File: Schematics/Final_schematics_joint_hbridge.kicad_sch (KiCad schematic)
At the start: 42 parts, among them J1 FVOL, J2 RVOL, J3 L-R, J4 ISP_Alike, J5 Conn_01x02_Pin, J6 F-R, J7 Header, Q5 Q_PMOS, Q6 Q_NMOS_GDS, Q7 Q_PMOS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

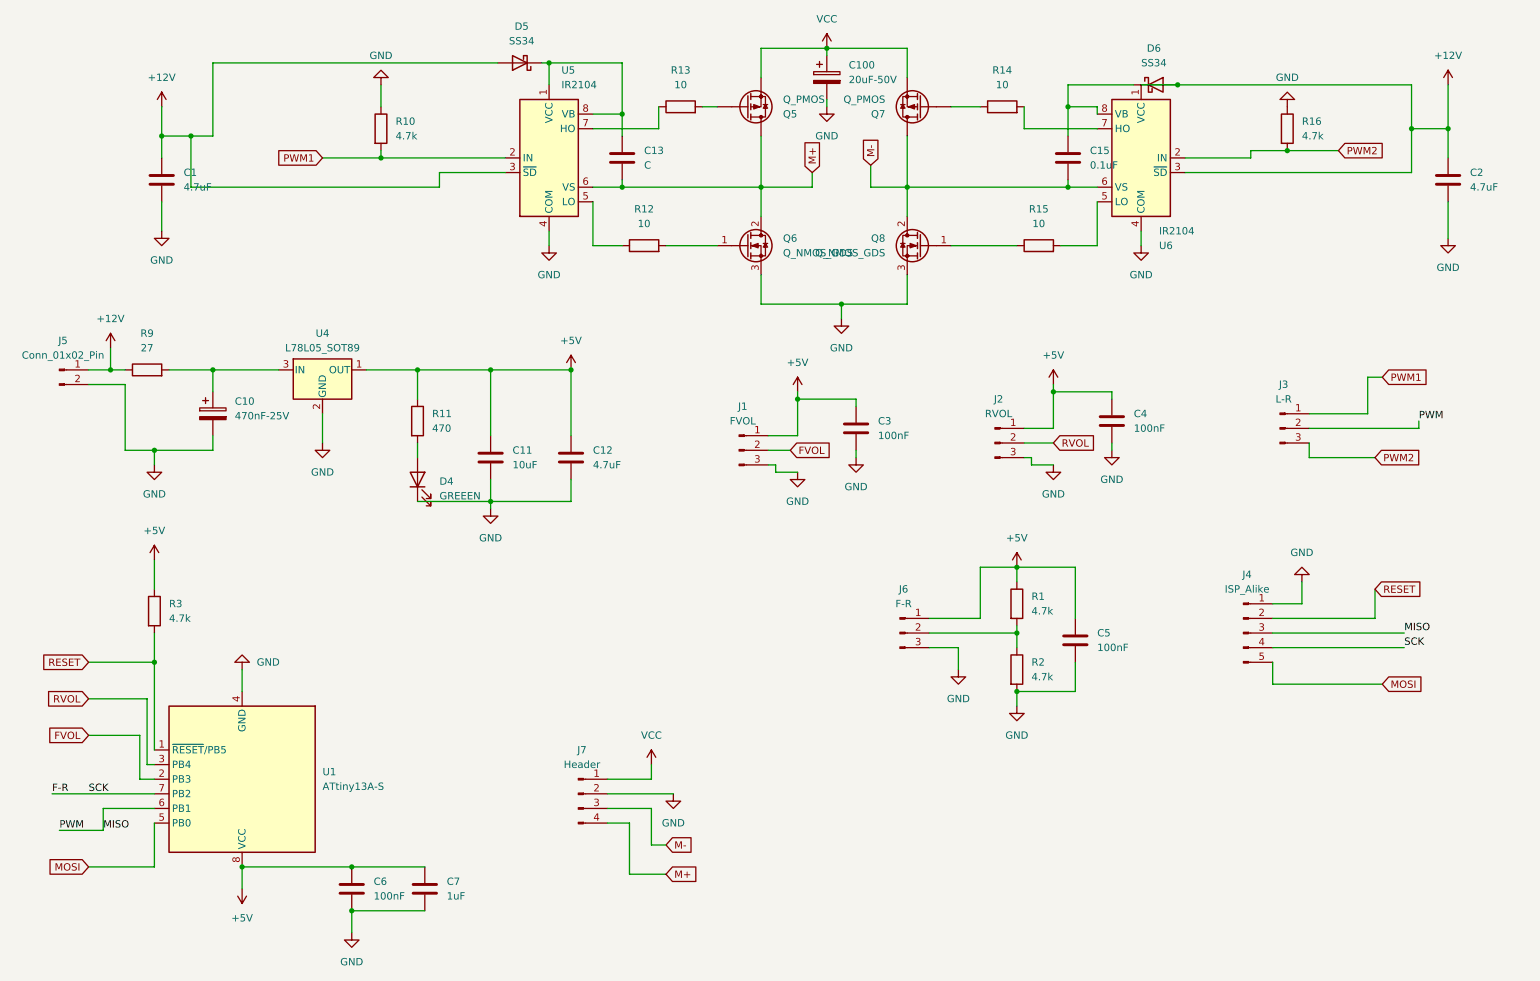
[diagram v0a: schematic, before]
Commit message: Revised schematic with KiCAD
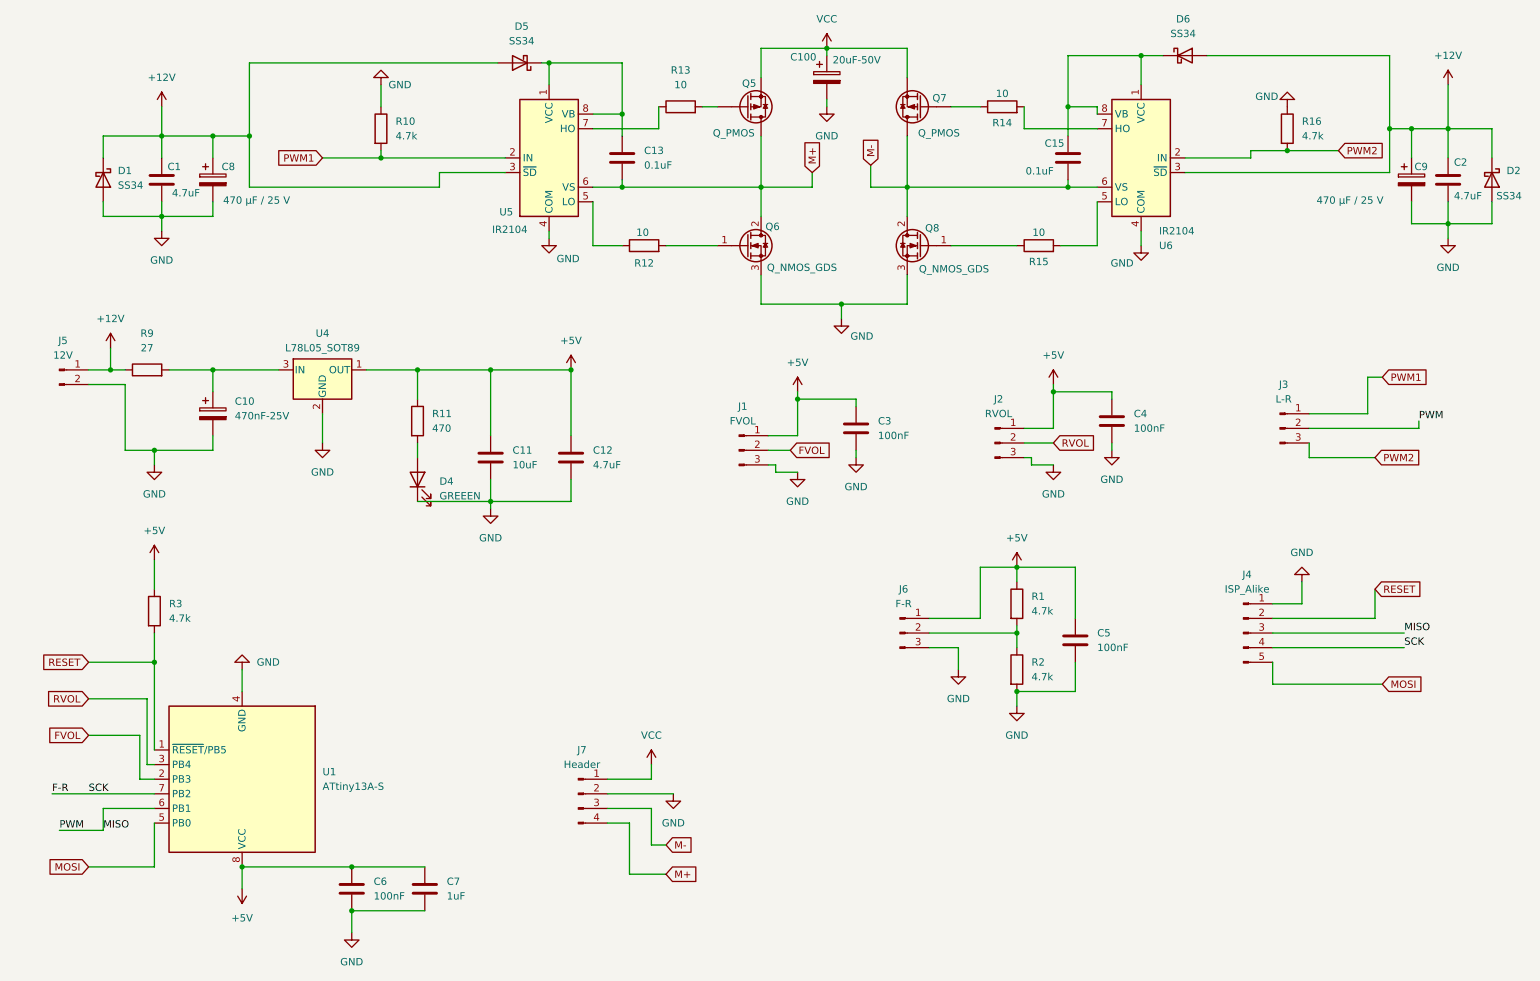
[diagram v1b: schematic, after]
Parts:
- added C8, C9: 470 µF / 25 V, symbol Device:C_Polarized
- added D1, D2: SS34, Diode_SMD:D_SMA, symbol Diode:SS34
- C13: value C -> 0.1uF
- J5: value Conn_01x02_Pin -> 12V
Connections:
- net +12V: now also C8.1, C9.1, D1.1 (K), D2.1 (K); no longer U6.1 (VCC)
- net GND: now also C8.2, C9.2, D1.2 (A), D2.2 (A)
- net at C15.1, D6.1 (K), U6.8 (VB): now also U6.1 (VCC)
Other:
- moved on the sheet: D6

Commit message: Resolve merge conflicts
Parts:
- added J8: Conn_01x01_Pin, symbol Connector:Conn_01x01_Pin
- added R_shunt: 0.05, symbol Device:R
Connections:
- net GND: now also R_shunt.2; no longer Q6.3 (S), Q8.3 (S)
- new net TorqueSensor: J8.1 (Pin_1), Q6.3 (S), Q8.3 (S), R_shunt.1
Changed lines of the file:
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@@
 	)
 	(junction
+		(at 165.1 72.39)
+		(diameter 0)
+		(color 0 0 0 0)
+	)
+	(junction
 		(at 91.44 83.82)
 		(diameter 0)
@@
 	)
 	(junction
-		(at 165.1 72.39)
+		(at 165.1 73.66)
 		(diameter 0)
 		(color 0 0 0 0)
@@
 	(wire
 		(pts
-			(xy 165.1 72.39) (xy 176.53 72.39)
-		)
-		(stroke
-			(width 0)
-			(type default)
-		)
-	)
-	(wire
-		(pts
 			(xy 195.58 118.11) (xy 195.58 120.65)
 		)
@@
 	(wire
 		(pts
+			(xy 250.19 76.2) (xy 257.81 76.2)
+		)
+		(stroke
+			(width 0)
+			(type default)
+		)
+	)
+	(wire
+		(pts
 			(xy 185.42 132.08) (xy 185.42 135.89)
 		)
@@
 	(wire
 		(pts
-			(xy 165.1 72.39) (xy 165.1 74.93)
-		)
-		(stroke
-			(width 0)
-			(type default)
-		)
-	)
-	(wire
-		(pts
 			(xy 278.13 46.99) (xy 278.13 41.91)
 		)
@@
 	(wire
 		(pts
+			(xy 165.1 73.66) (xy 182.88 73.66)
+		)
+		(stroke
+			(width 0)
+			(type default)
+		)
+	)
+	(wire
+		(pts
+			(xy 165.1 72.39) (xy 165.1 73.66)
+		)
+		(stroke
+			(width 0)
+			(type default)
+		)
+	)
+	(wire
+		(pts
 			(xy 132.08 166.37) (xy 134.62 166.37)
 		)
@@
 	(wire
 		(pts
+			(xy 165.1 81.28) (xy 165.1 83.82)
+		)
+		(stroke
+			(width 0)
+			(type default)
+		)
+	)
+	(wire
+		(pts
 			(xy 265.43 92.71) (xy 265.43 93.98)
 		)
@@
 	(wire
 		(pts
+			(xy 165.1 72.39) (xy 176.53 72.39)
+		)
+		(stroke
+			(width 0)
+			(type default)
+		)
+	)
+	(wire
+		(pts
 			(xy 240.03 138.43) (xy 259.08 138.43)
 		)
@@
 		)
 	)
+	(global_label "TorqueSensor"
+		(shape input)
+		(at 182.88 73.66 0)
+		(fields_autoplaced yes)
+		(effects
+			(font
+				(size 1.27 1.27)
+			)
+			(justify left)
+		)
+		(property "Intersheetrefs" "${INTERSHEET_REFS}"
+			(at 198.565 73.66 0)
+			(effects
+				(font
+					(size 1.27 1.27)
+				)
+				(justify left)
+				(hide yes)
+			)
+		)
+	)
 	(global_label "M-"
 		(shape input)
@@
 		)
 	)
+	(global_label "TorqueSensor"
+		(shape input)
+		(at 257.81 76.2 0)
+		(fields_autoplaced yes)
+		(effects
+			(font
+				(size 1.27 1.27)
+			)
+			(justify left)
+		)
+		(property "Intersheetrefs" "${INTERSHEET_REFS}"
+			(at 273.495 76.2 0)
+			(effects
+				(font
+					(size 1.27 1.27)
+				)
+				(justify left)
+				(hide yes)
+			)
+		)
+	)
 	(global_label "RVOL"
 		(shape input)
@@
 	(symbol
 		(lib_id "power:GND")
-		(at 165.1 74.93 0)
+		(at 165.1 83.82 0)
 		(unit 1)
 		(exclude_from_sim no)
@@
 		(dnp no)
 		(property "Reference" "#PWR028"
-			(at 165.1 81.28 0)
+			(at 165.1 90.17 0)
 			(effects
 				(font
@@
 		)
 		(property "Value" "GND"
-			(at 168.656 77.978 0)
+			(at 168.656 86.868 0)
 			(effects
 				(font
@@
 		)
 		(property "Footprint" ""
-			(at 165.1 74.93 0)
+			(at 165.1 83.82 0)
 			(effects
 				(font
@@
 		)
 		(property "Datasheet" ""
-			(at 165.1 74.93 0)
+			(at 165.1 83.82 0)
 			(effects
 				(font
@@
 		)
 		(property "Description" "Power symbol creates a global label with name \"GND\" , ground"
-			(at 165.1 74.93 0)
+			(at 165.1 83.82 0)
 			(effects
 				(font
@@
 	)
 	(symbol
+		(lib_id "Device:R")
+		(at 165.1 77.47 0)
+		(unit 1)
+		(exclude_from_sim no)
+		(in_bom yes)
+		(on_board yes)
+		(dnp no)
+		(fields_autoplaced yes)
+		(property "Reference" "R_shunt"
+			(at 167.64 76.1999 0)
+			(effects
+				(font
+					(size 1.27 1.27)
+				)
+				(justify left)
+			)
+		)
+		(property "Value" "0.05"
+			(at 167.64 78.7399 0)
+			(effects
+				(font
+					(size 1.27 1.27)
+				)
+				(justify left)
+			)
+		)
+		(property "Footprint" ""
+			(at 163.322 77.47 90)
+			(effects
+				(font
+					(size 1.27 1.27)
+				)
+				(hide yes)
+			)
+		)
+		(property "Datasheet" "~"
+			(at 165.1 77.47 0)
+			(effects
+				(font
+					(size 1.27 1.27)
+				)
+				(hide yes)
+			)
+		)
+		(property "Description" "Resistor"
+			(at 165.1 77.47 0)
+			(effects
+				(font
+					(size 1.27 1.27)
+				)
+				(hide yes)
+			)
+		)
+		(pin "2"
+		)
+		(pin "1"
+		)
+		(instances
+			(project ""
+				(path "/6b1e787a-9a3a-4b4c-81e6-12224e330815"
+					(reference "R_shunt")
+					(unit 1)
+				)
+			)
+		)
+	)
+	(symbol
 		(lib_id "power:GND")
 		(at 135.89 157.48 0)
@@
 					(unit 1)
 				)
+			)
+		)
+	)
+	(symbol
+		(lib_id "Connector:Conn_01x01_Pin")
+		(at 245.11 76.2 0)
+		(unit 1)
+		(exclude_from_sim no)
+		(in_bom yes)
+		(on_board yes)
+		(dnp no)
+		(fields_autoplaced yes)
+		(property "Reference" "J8"
+			(at 245.745 71.12 0)
+			(effects
+				(font
+					(size 1.27 1.27)
+				)
+			)
+		)
+		(property "Value" "Conn_01x01_Pin"
+			(at 245.745 73.66 0)
+			(effects
+				(font
+					(size 1.27 1.27)
+				)
+			)
+		)
+		(property "Footprint" ""
+			(at 245.11 76.2 0)
+			(effects
+				(font
+					(size 1.27 1.27)
+				)
+				(hide yes)
+			)
+		)
+		(property "Datasheet" "~"
+			(at 245.11 76.2 0)
+			(effects
+				(font
+					(size 1.27 1.27)
+				)
+				(hide yes)
+			)
+		)
+		(property "Description" "Generic connector, single row, 01x01, script generated"
+			(at 245.11 76.2 0)
+			(effects
+				(font
+					(size 1.27 1.27)
+				)
+				(hide yes)
+			)
+		)
+		(pin "1"
+		)
+		(instances
+			(project ""
+				(path "/6b1e787a-9a3a-4b4c-81e6-12224e330815"
+					(reference "J8")
+					(unit 1)
+				)

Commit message: Resolve merge conflicts
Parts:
- removed J8: Conn_01x01_Pin, symbol Connector:Conn_01x01_Pin
- added TorqueSensor: V_shunt, symbol Connector:Conn_01x02_Pin
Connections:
- net GND: now also TorqueSensor.2 (Pin_2)
- net TorqueSensor: now also TorqueSensor.1 (Pin_1)
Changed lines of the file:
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@@
 	(wire
 		(pts
-			(xy 250.19 76.2) (xy 257.81 76.2)
+			(xy 185.42 132.08) (xy 185.42 135.89)
 		)
 		(stroke
@@
 	(wire
 		(pts
-			(xy 185.42 132.08) (xy 185.42 135.89)
+			(xy 45.72 154.94) (xy 43.18 154.94)
 		)
 		(stroke
@@
 	(wire
 		(pts
-			(xy 45.72 154.94) (xy 43.18 154.94)
+			(xy 134.62 62.23) (xy 143.51 62.23)
 		)
 		(stroke
@@
 	(wire
 		(pts
-			(xy 134.62 62.23) (xy 143.51 62.23)
+			(xy 204.47 52.07) (xy 209.55 52.07)
 		)
 		(stroke
@@
 	(wire
 		(pts
-			(xy 204.47 52.07) (xy 209.55 52.07)
+			(xy 246.38 72.39) (xy 250.19 72.39)
 		)
 		(stroke
@@
 	(wire
 		(pts
+			(xy 246.38 74.93) (xy 250.19 74.93)
+		)
+		(stroke
+			(width 0)
+			(type default)
+		)
+	)
+	(wire
+		(pts
 			(xy 198.12 100.33) (xy 201.93 100.33)
 		)
@@
 	(wire
 		(pts
+			(xy 250.19 74.93) (xy 250.19 76.2)
+		)
+		(stroke
+			(width 0)
+			(type default)
+		)
+	)
+	(wire
+		(pts
 			(xy 184.15 38.1) (xy 189.23 38.1)
 		)
@@
 	(global_label "TorqueSensor"
 		(shape input)
-		(at 257.81 76.2 0)
+		(at 250.19 72.39 0)
 		(fields_autoplaced yes)
 		(effects
@@
 		)
 		(property "Intersheetrefs" "${INTERSHEET_REFS}"
-			(at 273.495 76.2 0)
+			(at 265.875 72.39 0)
 			(effects
 				(font
@@
 	)
 	(symbol
+		(lib_id "Connector:Conn_01x02_Pin")
+		(at 241.3 72.39 0)
+		(unit 1)
+		(exclude_from_sim no)
+		(in_bom yes)
+		(on_board yes)
+		(dnp no)
+		(fields_autoplaced yes)
+		(property "Reference" "TorqueSensor"
+			(at 241.935 67.31 0)
+			(effects
+				(font
+					(size 1.27 1.27)
+				)
+			)
+		)
+		(property "Value" "V_shunt"
+			(at 241.935 69.85 0)
+			(effects
+				(font
+					(size 1.27 1.27)
+				)
+			)
+		)
+		(property "Footprint" ""
+			(at 241.3 72.39 0)
+			(effects
+				(font
+					(size 1.27 1.27)
+				)
+				(hide yes)
+			)
+		)
+		(property "Datasheet" "~"
+			(at 241.3 72.39 0)
+			(effects
+				(font
+					(size 1.27 1.27)
+				)
+				(hide yes)
+			)
+		)
+		(property "Description" "Generic connector, single row, 01x02, script generated"
+			(at 241.3 72.39 0)
+			(effects
+				(font
+					(size 1.27 1.27)
+				)
+				(hide yes)
+			)
+		)
+		(pin "1"
+		)
+		(pin "2"
+		)
+		(instances
+			(project "joint_hbridge"
+				(path "/6b1e787a-9a3a-4b4c-81e6-12224e330815"
+					(reference "TorqueSensor")
+					(unit 1)
+				)
+			)
+		)
+	)
+	(symbol
 		(lib_id "Device:R")
 		(at 165.1 77.47 0)
@@
 	)
 	(symbol
-		(lib_id "Connector:Conn_01x01_Pin")
-		(at 245.11 76.2 0)
+		(lib_id "Device:C")
+		(at 205.74 130.81 0)
 		(unit 1)
 		(exclude_from_sim no)
@@
 		(dnp no)
 		(fields_autoplaced yes)
-		(property "Reference" "J8"
-			(at 245.745 71.12 0)
+		(property "Reference" "C5"
+			(at 209.55 129.5399 0)
 			(effects
 				(font
 					(size 1.27 1.27)
 				)
+				(justify left)
 			)
 		)
-		(property "Value" "Conn_01x01_Pin"
-			(at 245.745 73.66 0)
+		(property "Value" "100nF"
+			(at 209.55 132.0799 0)
 			(effects
 				(font
 					(size 1.27 1.27)
 				)
+				(justify left)
 			)
 		)
 		(property "Footprint" ""
-			(at 245.11 76.2 0)
+			(at 206.7052 134.62 0)
 			(effects
 				(font
@@
 		)
 		(property "Datasheet" "~"
-			(at 245.11 76.2 0)
+			(at 205.74 130.81 0)
 			(effects
 				(font
@@
 			)
 		)
-		(property "Description" "Generic connector, single row, 01x01, script generated"
-			(at 245.11 76.2 0)
+		(property "Description" "Unpolarized capacitor"
+			(at 205.74 130.81 0)
 			(effects
 				(font
@@
 		(pin "1"
 		)
+		(pin "2"
+		)
 		(instances
-			(project ""
+			(project "joint_hbridge"
 				(path "/6b1e787a-9a3a-4b4c-81e6-12224e330815"
-					(reference "J8")
+					(reference "C5")
 					(unit 1)
 				)
@@
 	)
 	(symbol
-		(lib_id "Device:C")
-		(at 205.74 130.81 0)
+		(lib_id "Connector:Conn_01x03_Pin")
+		(at 147.32 97.79 0)
 		(unit 1)
 		(exclude_from_sim no)
@@
 		(dnp no)
 		(fields_autoplaced yes)
-		(property "Reference" "C5"
-			(at 209.55 129.5399 0)
+		(property "Reference" "J1"
+			(at 147.955 90.17 0)
 			(effects
 				(font
 					(size 1.27 1.27)
 				)
-				(justify left)
 			)
 		)
-		(property "Value" "100nF"
-			(at 209.55 132.0799 0)
+		(property "Value" "FVOL"
+			(at 147.955 92.71 0)
 			(effects
 				(font
 					(size 1.27 1.27)
 				)
-				(justify left)
 			)
 		)
 		(property "Footprint" ""
-			(at 206.7052 134.62 0)
+			(at 147.32 97.79 0)
 			(effects
 				(font
@@
 		)
 		(property "Datasheet" "~"
-			(at 205.74 130.81 0)
+			(at 147.32 97.79 0)
 			(effects
 				(font
@@
 			)
 		)
-		(property "Description" "Unpolarized capacitor"
-			(at 205.74 130.81 0)
+		(property "Description" "Generic connector, single row, 01x03, script generated"
+			(at 147.32 97.79 0)
 			(effects
 				(font
@@
 		(pin "1"
 		)
+		(pin "3"
+		)
 		(pin "2"
 		)
 		(instances
-			(project "joint_hbridge"
+			(project ""
 				(path "/6b1e787a-9a3a-4b4c-81e6-12224e330815"
-					(reference "C5")
+					(reference "J1")
 					(unit 1)
 				)
@@
 	)
 	(symbol
-		(lib_id "Connector:Conn_01x03_Pin")
-		(at 147.32 97.79 0)
+		(lib_id "power:GND")
+		(at 250.19 76.2 0)
 		(unit 1)
 		(exclude_from_sim no)
@@
 		(on_board yes)
 		(dnp no)
-		(fields_autoplaced yes)
-		(property "Reference" "J1"
-			(at 147.955 90.17 0)
+		(property "Reference" "#PWR033"
+			(at 250.19 82.55 0)
 			(effects
 				(font
 					(size 1.27 1.27)
 				)
+				(hide yes)
 			)
 		)
-		(property "Value" "FVOL"
-			(at 147.955 92.71 0)
+		(property "Value" "GND"
+			(at 253.746 79.248 0)
 			(effects
 				(font
@@
 		)
 		(property "Footprint" ""
-			(at 147.32 97.79 0)
+			(at 250.19 76.2 0)
 			(effects
 				(font
@@
 			)
 		)
-		(property "Datasheet" "~"
-			(at 147.32 97.79 0)
+		(property "Datasheet" ""
+			(at 250.19 76.2 0)
 			(effects
 				(font
@@
 			)
 		)
-		(property "Description" "Generic connector, single row, 01x03, script generated"
-			(at 147.32 97.79 0)
+		(property "Description" "Power symbol creates a global label with name \"GND\" , ground"
+			(at 250.19 76.2 0)
 			(effects
 				(font
@@
 		(pin "1"
 		)
-		(pin "3"
-		)
-		(pin "2"
-		)
 		(instances
-			(project ""
+			(project "joint_hbridge"
 				(path "/6b1e787a-9a3a-4b4c-81e6-12224e330815"
-					(reference "J1")
+					(reference "#PWR033")
 					(unit 1)
 				)

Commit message: Resolve merge conflicts
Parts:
- removed Q5, Q7: Q_PMOS, symbol Device:Q_PMOS
- added D3, D7, D8, D9: SS36, Diode_SMD:D_SMA, symbol Diode:SS36
- added Q1, Q2: Q_NMOS_GDS, symbol Transistor_FET:Q_NMOS_GDS
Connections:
- net M+: now also D3.2 (A), D9.1 (K), Q1.2 (D)
- net M-: now also D7.2 (A), D8.1 (K), Q2.2 (D)
- net TorqueSensor: now also D8.2 (A), D9.2 (A)
- net VCC: now also D3.1 (K), D7.1 (K), Q1.3 (S), Q2.3 (S)
- net at R13.2: now also Q1.1 (G)
- net at R14.1: now also Q2.1 (G)

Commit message: Resolve merge conflicts
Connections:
- net M+: now also Q1.3 (S); no longer Q1.2 (D)
- net M-: now also Q2.3 (S); no longer Q2.2 (D)
- net VCC: now also Q1.2 (D), Q2.2 (D); no longer Q1.3 (S), Q2.3 (S)
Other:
- moved on the sheet: Q2
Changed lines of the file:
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@@
 		(lib_id "Transistor_FET:Q_NMOS_GDS")
 		(at 148.59 38.1 0)
-		(mirror x)
 		(unit 1)
 		(exclude_from_sim no)
@@
 		(dnp no)
 		(property "Reference" "Q1"
-			(at 151.892 41.402 0)
+			(at 151.892 34.798 0)
 			(effects
 				(font
@@
 		)
 		(property "Value" "Q_NMOS_GDS"
-			(at 152.146 34.29 0)
-			(effects
-				(font
-					(size 1.27 1.27)
-				)
-				(justify left)
-			)
-		)
-		(property "Footprint" ""
-			(at 153.67 40.64 0)
+			(at 152.146 41.91 0)
+			(effects
+				(font
+					(size 1.27 1.27)
+				)
+				(justify left)
+			)
+		)
+		(property "Footprint" ""
+			(at 153.67 35.56 0)
 			(effects
 				(font
@@
 	(symbol
 		(lib_id "Transistor_FET:Q_NMOS_GDS")
-		(at 179.07 38.1 180)
+		(at 179.07 38.1 0)
+		(mirror y)
 		(unit 1)
 		(exclude_from_sim no)
@@
 		(dnp no)
 		(property "Reference" "Q2"
-			(at 182.118 41.148 0)
+			(at 182.118 35.052 0)
 			(effects
 				(font
@@
 		)
 		(property "Value" "Q_NMOS_GDS"
-			(at 190.754 34.036 0)
-			(effects
-				(font
-					(size 1.27 1.27)
-				)
-				(justify left)
-			)
-		)
-		(property "Footprint" ""
-			(at 173.99 40.64 0)
-			(effects
-				(font
+			(at 190.754 42.164 0)
+			(effects
+				(font
+					(size 1.27 1.27)
+				)
+				(justify left)
+			)
+		)
+		(property "Footprint" ""
+			(at 173.99 35.56 0)
+			(effects
+				(font
